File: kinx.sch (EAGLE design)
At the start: 45 parts, among them T1 MCP1825S

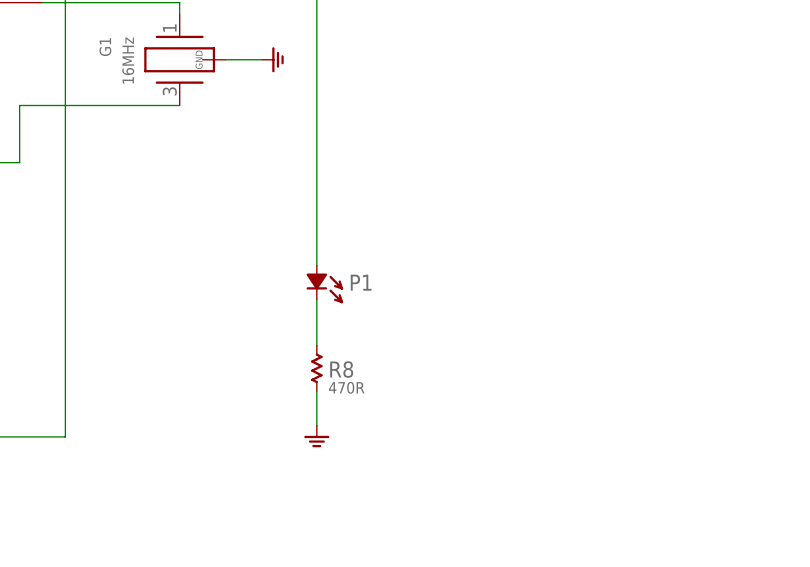
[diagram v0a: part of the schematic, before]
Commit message: fix silkscreen for power LED
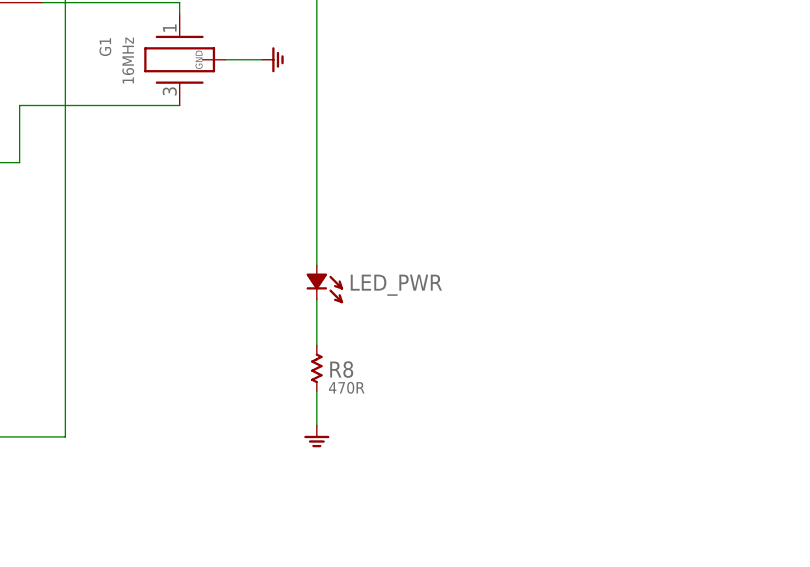
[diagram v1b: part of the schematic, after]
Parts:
- renumbered P1 to LED_PWR
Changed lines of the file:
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@@
 <part name="GND3" library="t32_ref" deviceset="GND" device=""/>
 <part name="GND2" library="t32_ref" deviceset="GND" device=""/>
-<part name="P1" library="t32_ref" deviceset="LED" device=""/>
+<part name="LED_PWR" library="t32_ref" deviceset="LED" device=""/>
 <part name="GND21" library="t32_ref" deviceset="GND" device=""/>
 <part name="S1" library="t32_ref" deviceset="TACT_SWITCH" device=""/>
@@
 <instance part="GND3" gate="1" x="-281.686" y="91.44"/>
 <instance part="GND2" gate="1" x="-286.766" y="91.44"/>
-<instance part="P1" gate="G$1" x="-93.98" y="-24.13"/>
+<instance part="LED_PWR" gate="G$1" x="-93.98" y="-24.13"/>
 <instance part="GND21" gate="1" x="-93.98" y="-40.64"/>
 <instance part="S1" gate="G$1" x="-161.29" y="-96.52" rot="R90"/>
@@
 <net name="N$41" class="0">
 <segment>
-<pinref part="P1" gate="G$1" pin="+"/>
+<pinref part="LED_PWR" gate="G$1" pin="+"/>
 <wire x1="-93.98" y1="-21.59" x2="-93.98" y2="91.44" width="0.1524" layer="91"/>
 <pinref part="U$1" gate="G$1" pin="PTC3"/>
@@
 <segment>
 <pinref part="R8" gate="G$1" pin="2"/>
-<pinref part="P1" gate="G$1" pin="-"/>
+<pinref part="LED_PWR" gate="G$1" pin="-"/>
 <wire x1="-93.98" y1="-25.4" x2="-93.98" y2="-30.48" width="0.1524" layer="91"/>
 </segment>

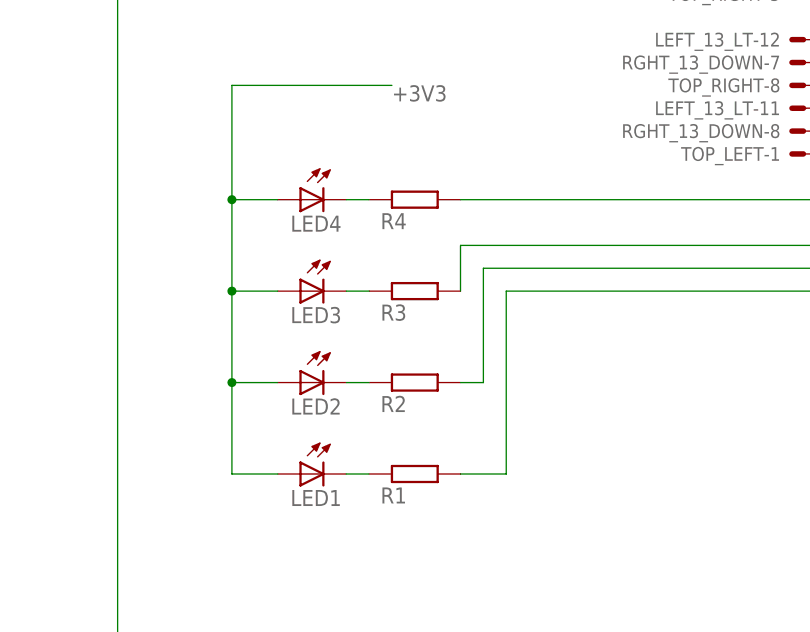
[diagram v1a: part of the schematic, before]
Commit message: use 10K resistors to drive the LEDs
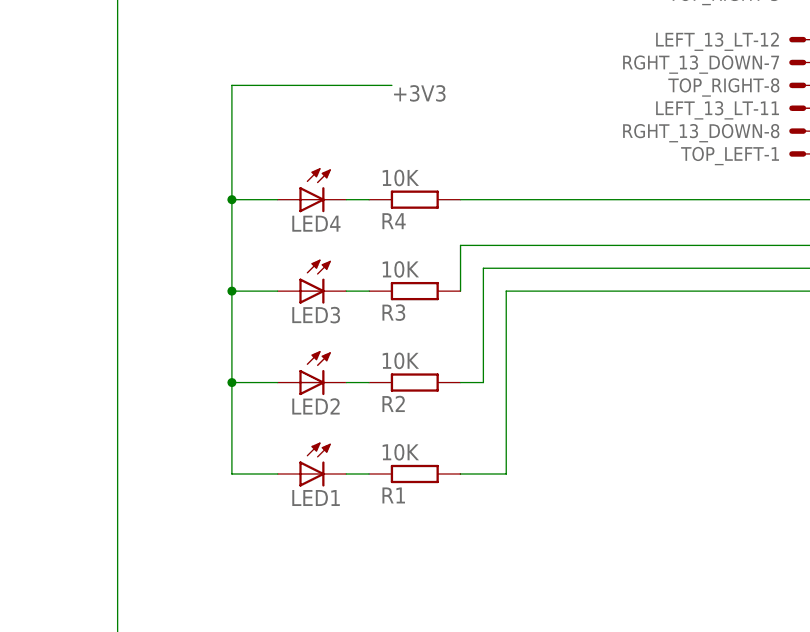
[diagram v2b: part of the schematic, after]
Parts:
- R1, R2, R3, R4: value (none) -> 10K
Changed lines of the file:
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@@
 <attribute name="OC_MOUSER" value="604-APT3216QBC/D"/>
 </part>
-<part name="R1" library="rcl" deviceset="R-EU_" device="R1206"/>
-<part name="R2" library="rcl" deviceset="R-EU_" device="R1206"/>
-<part name="R3" library="rcl" deviceset="R-EU_" device="R1206"/>
-<part name="R4" library="rcl" deviceset="R-EU_" device="R1206"/>
+<part name="R1" library="rcl" deviceset="R-EU_" device="R1206" value="10K"/>
+<part name="R2" library="rcl" deviceset="R-EU_" device="R1206" value="10K"/>
+<part name="R3" library="rcl" deviceset="R-EU_" device="R1206" value="10K"/>
+<part name="R4" library="rcl" deviceset="R-EU_" device="R1206" value="10K"/>
 <part name="H1" library="holes" deviceset="MOUNT-PAD-ROUND" device="4.1"/>
 <part name="MKL04Z32VLC4" library="t32_ref" deviceset="MKL04Z32VLC4" device="" value="MKL04Z32VLC4"/>

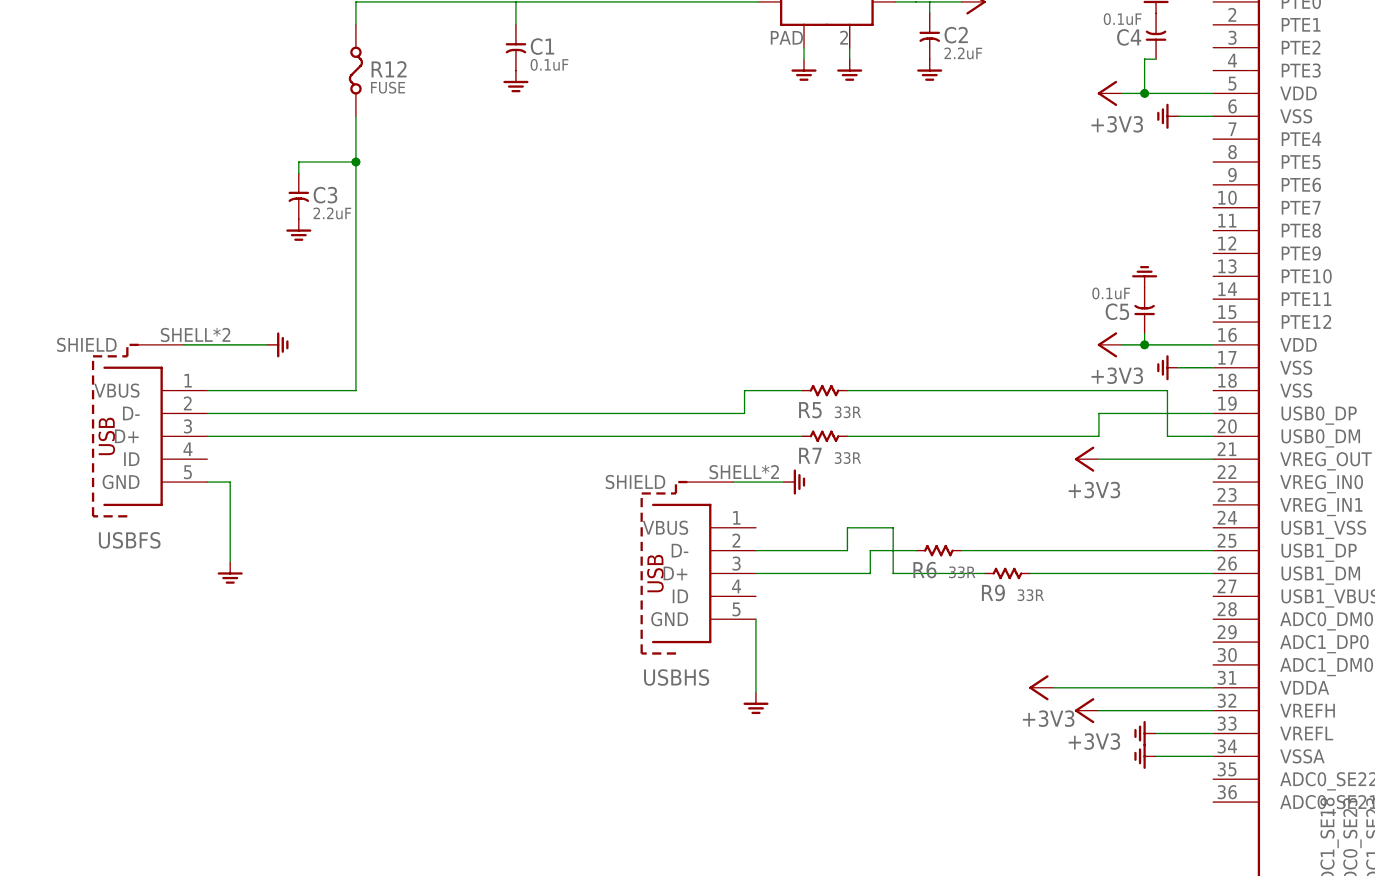
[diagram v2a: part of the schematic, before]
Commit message: Switch USB connector from Würth (1.0mm PCB) to Molex (1.5mm PCB)
The Würth ones are incompatible with our PCB thickness — they can just barely be
soldered, and are loose after just a few connections.
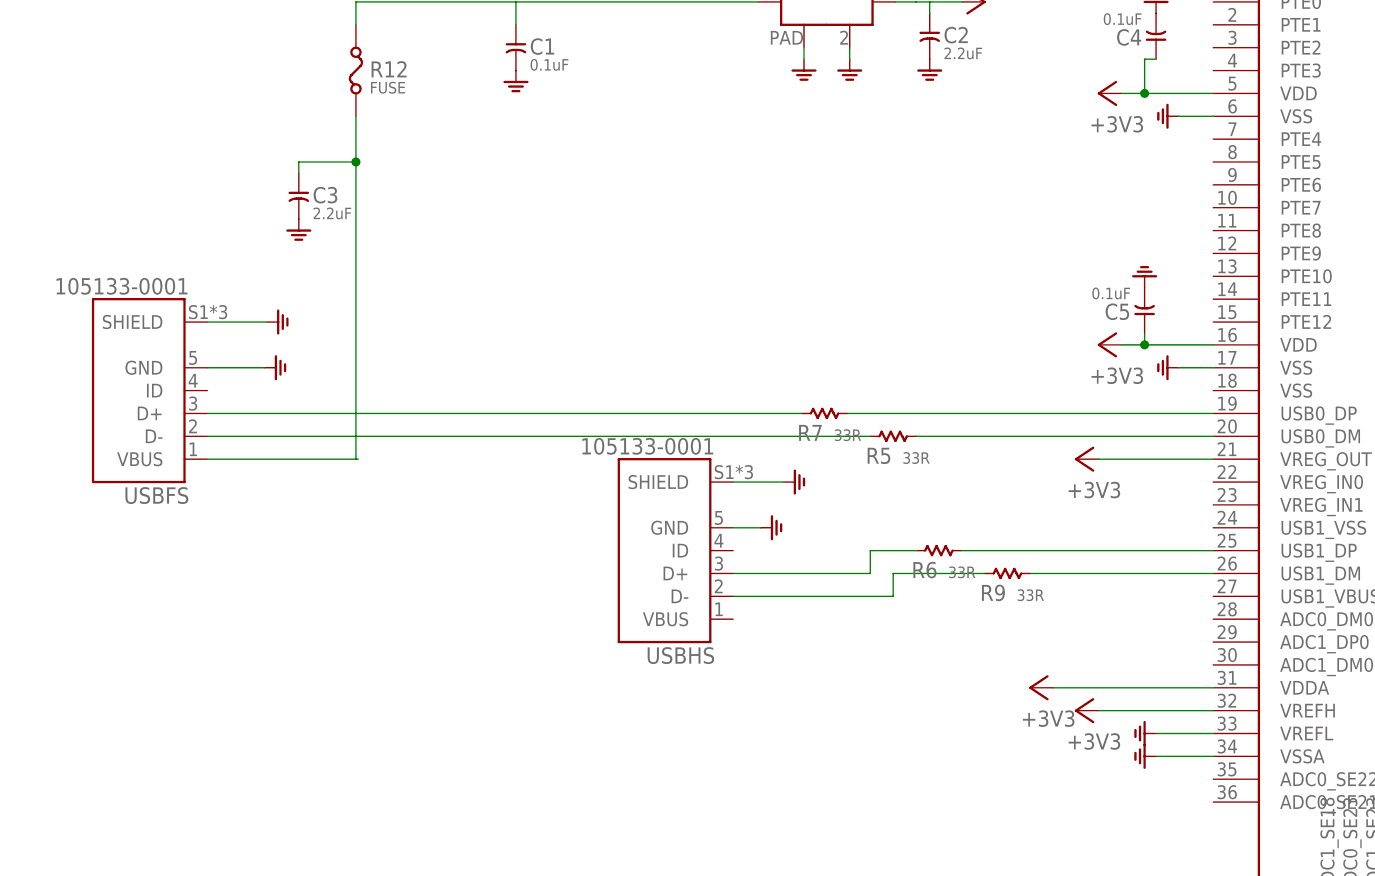
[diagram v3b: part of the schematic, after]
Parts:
- USBFS, USBHS: value (none) -> 105133-0001; device wurth-io-rev17e:614105150721 -> molex-105133-0001:105133-0001; DIGIKEY 732-5958-1-ND -> WM9734CT-ND; OC_MOUSER 710-614105150721 -> 538-105133-0001
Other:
- moved on the sheet: R5, R7
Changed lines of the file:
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@@
 <part name="GND15" library="t32_ref" deviceset="GND" device=""/>
 <part name="GND12" library="t32_ref" deviceset="GND" device=""/>
-<part name="USBFS" library="wurth-io-rev17e" deviceset="614105150721" device="">
-<attribute name="DIGIKEY" value="732-5958-1-ND"/>
-<attribute name="OC_MOUSER" value="710-614105150721"/>
+<part name="USBFS" library="molex-105133-0001" deviceset="105133-0001" device="">
+<attribute name="DIGIKEY" value="WM9734CT-ND"/>
+<attribute name="OC_MOUSER" value="538-105133-0001"/>
 </part>
-<part name="USBHS" library="wurth-io-rev17e" deviceset="614105150721" device="">
-<attribute name="DIGIKEY" value="732-5958-1-ND"/>
-<attribute name="OC_MOUSER" value="710-614105150721"/>
+<part name="USBHS" library="molex-105133-0001" deviceset="105133-0001" device="">
+<attribute name="DIGIKEY" value="WM9734CT-ND"/>
+<attribute name="OC_MOUSER" value="538-105133-0001"/>
 </part>
 <part name="+3V1" library="supply1" library_urn="urn:adsk.eagle:library:371" deviceset="+3V3" device=""/>
@@
 <instance part="GND14" gate="1" x="-177.8" y="-85.09" rot="R90"/>
 <instance part="GND4" gate="1" x="-272.796" y="91.44"/>
-<instance part="R5" gate="G$1" x="-284.48" y="55.88"/>
+<instance part="R5" gate="G$1" x="-276.86" y="50.8"/>
 <instance part="R8" gate="G$1" x="-93.98" y="-33.02" smashed="yes" rot="R90">
 <attribute name="NAME" x="-92.71" y="-34.036" size="1.778" layer="95" ratio="10"/>
 <attribute name="VALUE" x="-92.71" y="-35.814" size="1.27" layer="96" ratio="10"/>
 </instance>
-<instance part="R7" gate="G$1" x="-284.48" y="50.8"/>
-<instance part="GND9" gate="1" x="-350.52" y="35.56"/>
-<instance part="GND10" gate="1" x="-345.186" y="60.96" rot="R90"/>
+<instance part="R7" gate="G$1" x="-284.48" y="53.34"/>
+<instance part="GND9" gate="1" x="-345.44" y="58.42" rot="R90"/>
+<instance part="GND10" gate="1" x="-345.186" y="63.5" rot="R90"/>
 <instance part="GND5" gate="1" x="-342.9" y="73.66"/>
 <instance part="T1" gate="G$1" x="-284.226" y="99.06">
@@
 <attribute name="OC_MOUSER" x="-182.88" y="53.34" size="1.778" layer="96" display="off"/>
 </instance>
-<instance part="GND8" gate="1" x="-292.1" y="21.082"/>
+<instance part="GND8" gate="1" x="-290.322" y="40.64" rot="R90"/>
 <instance part="GND11" gate="1" x="-287.782" y="45.72" rot="R90"/>
 <instance part="R6" gate="G$1" x="-271.78" y="38.1"/>
@@
 <instance part="GND15" gate="1" x="-142.24" y="-15.24"/>
 <instance part="GND12" gate="1" x="-98.806" y="1.27" rot="R90"/>
-<instance part="USBFS" gate="G$1" x="-360.68" y="50.8" rot="R180">
-<attribute name="DIGIKEY" x="-360.68" y="50.8" size="1.778" layer="96" rot="R180" display="off"/>
-<attribute name="OC_MOUSER" x="-360.68" y="50.8" size="1.778" layer="96" rot="R180" display="off"/>
-</instance>
-<instance part="USBHS" gate="G$1" x="-299.72" y="35.56" rot="R180">
-<attribute name="DIGIKEY" x="-299.72" y="35.56" size="1.778" layer="96" rot="R180" display="off"/>
-<attribute name="OC_MOUSER" x="-299.72" y="35.56" size="1.778" layer="96" rot="R180" display="off"/>
+<instance part="USBFS" gate="G$1" x="-360.68" y="55.88" rot="R180">
+<attribute name="DIGIKEY" x="-360.68" y="55.88" size="1.778" layer="96" rot="R180" display="off"/>
+<attribute name="OC_MOUSER" x="-360.68" y="55.88" size="1.778" layer="96" rot="R180" display="off"/>
+</instance>
+<instance part="USBHS" gate="G$1" x="-302.26" y="38.1" rot="R180">
+<attribute name="DIGIKEY" x="-302.26" y="38.1" size="1.778" layer="96" rot="R180" display="off"/>
+<attribute name="OC_MOUSER" x="-302.26" y="38.1" size="1.778" layer="96" rot="R180" display="off"/>
 </instance>
 <instance part="+3V1" gate="G$1" x="-266.7" y="99.06" rot="R270"/>
@@
 </segment>
 <segment>
-<pinref part="GND8" gate="1" pin="GND"/>
-<pinref part="USBHS" gate="G$1" pin="GND"/>
-<wire x1="-292.1" y1="22.352" x2="-292.1" y2="30.48" width="0.1524" layer="91"/>
-</segment>
-<segment>
 <pinref part="U$1" gate="G$1" pin="VSS@6"/>
 <pinref part="GND15" gate="1" pin="GND"/>
@@
 </segment>
 <segment>
-<pinref part="GND9" gate="1" pin="GND"/>
-<wire x1="-350.52" y1="36.83" x2="-350.52" y2="45.72" width="0.1524" layer="91"/>
-<pinref part="USBFS" gate="G$1" pin="GND"/>
-<wire x1="-350.52" y1="45.72" x2="-353.06" y2="45.72" width="0.1524" layer="91"/>
-</segment>
-<segment>
 <pinref part="GND10" gate="1" pin="GND"/>
 <pinref part="USBFS" gate="G$1" pin="SHIELD"/>
-<wire x1="-346.456" y1="60.96" x2="-355.6" y2="60.96" width="0.1524" layer="91"/>
+<wire x1="-346.456" y1="63.5" x2="-353.06" y2="63.5" width="0.1524" layer="91"/>
 </segment>
 <segment>
@@
 <pinref part="C13" gate="G$1" pin="2"/>
 <pinref part="GND37" gate="1" pin="GND"/>
+</segment>
+<segment>
+<pinref part="GND9" gate="1" pin="GND"/>
+<pinref part="USBFS" gate="G$1" pin="GND"/>
+<wire x1="-346.71" y1="58.42" x2="-353.06" y2="58.42" width="0.1524" layer="91"/>
+</segment>
+<segment>
+<pinref part="USBHS" gate="G$1" pin="GND"/>
+<pinref part="GND8" gate="1" pin="GND"/>
+<wire x1="-294.64" y1="40.64" x2="-291.592" y2="40.64" width="0.1524" layer="91"/>
 </segment>
 </net>
@@
 <segment>
 <pinref part="R7" gate="G$1" pin="2"/>
-<wire x1="-254" y1="50.8" x2="-281.94" y2="50.8" width="0.1524" layer="91"/>
+<wire x1="-241.3" y1="53.34" x2="-281.94" y2="53.34" width="0.1524" layer="91"/>
 <pinref part="U$1" gate="G$1" pin="USB0_DP"/>
-<wire x1="-241.3" y1="53.34" x2="-254" y2="53.34" width="0.1524" layer="91"/>
-<wire x1="-254" y1="53.34" x2="-254" y2="50.8" width="0.1524" layer="91"/>
 </segment>
 </net>
@@
 <segment>
 <pinref part="R7" gate="G$1" pin="1"/>
-<wire x1="-287.02" y1="50.8" x2="-353.06" y2="50.8" width="0.1524" layer="91"/>
+<wire x1="-287.02" y1="53.34" x2="-353.06" y2="53.34" width="0.1524" layer="91"/>
 <pinref part="USBFS" gate="G$1" pin="D+"/>
 </segment>
@@
 <net name="D0_N" class="1">
 <segment>
-<wire x1="-353.06" y1="53.34" x2="-293.37" y2="53.34" width="0.1524" layer="91"/>
-<wire x1="-293.37" y1="53.34" x2="-293.37" y2="55.88" width="0.1524" layer="91"/>
+<wire x1="-353.06" y1="50.8" x2="-279.4" y2="50.8" width="0.1524" layer="91"/>
 <pinref part="R5" gate="G$1" pin="1"/>
-<wire x1="-293.37" y1="55.88" x2="-287.02" y2="55.88" width="0.1524" layer="91"/>
 <pinref part="USBFS" gate="G$1" pin="D-"/>
 </segment>
@@
 <net name="N$29" class="2">
 <segment>
-<wire x1="-353.06" y1="55.88" x2="-336.55" y2="55.88" width="0.1524" layer="91"/>
-<wire x1="-336.55" y1="55.88" x2="-336.55" y2="81.28" width="0.1524" layer="91"/>
 <pinref part="C3" gate="G$1" pin="1"/>
+<wire x1="-336.55" y1="48.26" x2="-336.55" y2="81.28" width="0.1524" layer="91"/>
 <wire x1="-336.55" y1="81.28" x2="-342.9" y2="81.28" width="0.1524" layer="91"/>
 <wire x1="-342.9" y1="81.28" x2="-342.9" y2="80.01" width="0.1524" layer="91"/>
@@
 <wire x1="-336.55" y1="81.28" x2="-336.55" y2="86.36" width="0.1524" layer="91"/>
 <junction x="-336.55" y="81.28"/>
+<wire x1="-336.55" y1="48.26" x2="-336.296" y2="48.26" width="0.1524" layer="91"/>
 <pinref part="USBFS" gate="G$1" pin="VBUS"/>
+<wire x1="-336.55" y1="48.26" x2="-353.06" y2="48.26" width="0.1524" layer="91"/>
 </segment>
 </net>
@@
 <segment>
 <pinref part="U$1" gate="G$1" pin="USB0_DM"/>
-<wire x1="-241.3" y1="50.8" x2="-246.38" y2="50.8" width="0.1524" layer="91"/>
-<wire x1="-246.38" y1="50.8" x2="-246.38" y2="55.88" width="0.1524" layer="91"/>
 <pinref part="R5" gate="G$1" pin="2"/>
-<wire x1="-246.38" y1="55.88" x2="-281.94" y2="55.88" width="0.1524" layer="91"/>
+<wire x1="-241.3" y1="50.8" x2="-274.32" y2="50.8" width="0.1524" layer="91"/>
 </segment>
 </net>
@@
 <net name="D1_P" class="1">
 <segment>
-<wire x1="-292.1" y1="35.56" x2="-279.4" y2="35.56" width="0.1524" layer="91"/>
+<wire x1="-294.64" y1="35.56" x2="-279.4" y2="35.56" width="0.1524" layer="91"/>
 <wire x1="-279.4" y1="35.56" x2="-279.4" y2="38.1" width="0.1524" layer="91"/>
 <pinref part="R6" gate="G$1" pin="1"/>
@@
 <pinref part="R9" gate="G$1" pin="1"/>
 <wire x1="-266.7" y1="35.56" x2="-276.86" y2="35.56" width="0.1524" layer="91"/>
-<wire x1="-276.86" y1="35.56" x2="-276.86" y2="40.64" width="0.1524" layer="91"/>
-<wire x1="-276.86" y1="40.64" x2="-281.94" y2="40.64" width="0.1524" layer="91"/>
-<wire x1="-281.94" y1="40.64" x2="-281.94" y2="38.1" width="0.1524" layer="91"/>
+<wire x1="-276.86" y1="35.56" x2="-276.86" y2="33.02" width="0.1524" layer="91"/>
 <pinref part="USBHS" gate="G$1" pin="D-"/>
-<wire x1="-281.94" y1="38.1" x2="-292.1" y2="38.1" width="0.1524" layer="91"/>
-</segment>
-</net>
+<wire x1="-276.86" y1="33.02" x2="-294.64" y2="33.02" width="0.1524" layer="91"/>
+</segment>
+</net>
